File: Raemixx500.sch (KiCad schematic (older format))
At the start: 2 parts

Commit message: Begin adding part numbers
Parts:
- V0, V1: MFG Name (none) -> SKIP; MFG Part Num (none) -> SKIP; Optional (none) -> SKIP
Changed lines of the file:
@@
 F 2 "Symbol:OSHW-Logo2_14.6x12mm_SilkScreen" H 6380 7640 50  0001 C CNN
 F 3 "" H 6380 7640 50  0001 C CNN
+F 4 "SKIP" H 6380 7640 50  0001 C CNN "MFG Name"
+F 5 "SKIP" H 6380 7640 50  0001 C CNN "MFG Part Num"
+F 6 "SKIP" H 6380 7640 50  0001 C CNN "Optional"
 	1    6380 7640
 	1    0    0    -1
@@
 F 2 "Symbol:KiCad-Logo2_12mm_SilkScreen" H 6380 7430 50  0001 C CNN
 F 3 "" H 6380 7430 50  0001 C CNN
+F 4 "SKIP" H 6380 7430 50  0001 C CNN "MFG Name"
+F 5 "SKIP" H 6380 7430 50  0001 C CNN "MFG Part Num"
+F 6 "SKIP" H 6380 7430 50  0001 C CNN "Optional"
 	1    6380 7430
 	1    0    0    -1

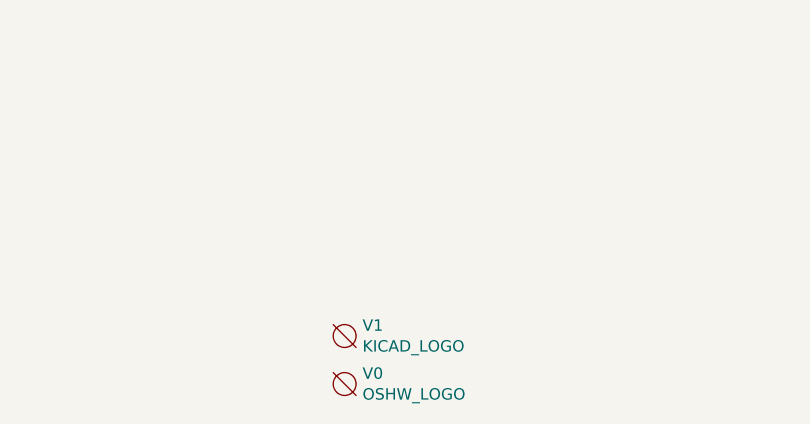
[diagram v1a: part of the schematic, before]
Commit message: Add EMI filter 3D models, add logo, re-add Rock Lobster (closes #15) Thanks to Szabó Zoltán and Workshopshed!
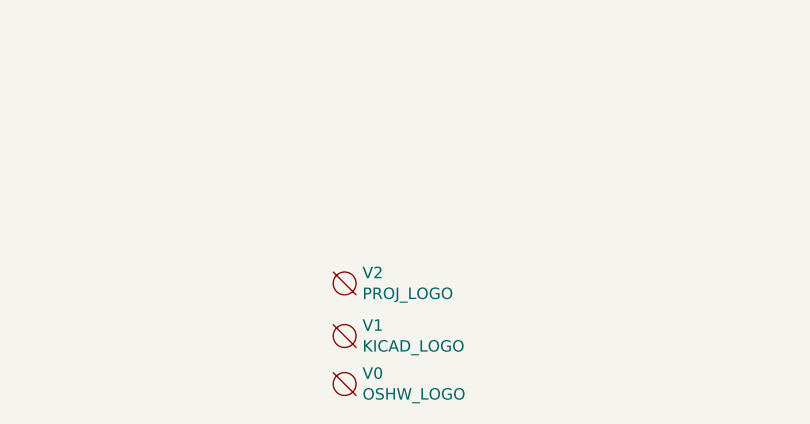
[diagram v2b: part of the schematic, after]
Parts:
- added V2: PROJ_LOGO, Raemixx500:Logo, symbol void:Void
- V1: footprint Symbol:KiCad-Logo2_12mm_SilkScreen -> Symbol:KiCad-Logo2_8mm_SilkScreen
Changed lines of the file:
@@
 F 0 "V1" H 6458 7476 50  0000 L CNN
 F 1 "KICAD_LOGO" H 6458 7385 50  0000 L CNN
-F 2 "Symbol:KiCad-Logo2_12mm_SilkScreen" H 6380 7430 50  0001 C CNN
+F 2 "Symbol:KiCad-Logo2_8mm_SilkScreen" H 6380 7430 50  0001 C CNN
 F 3 "" H 6380 7430 50  0001 C CNN
 F 4 "SKIP" H 6380 7430 50  0001 C CNN "MFG Name"
@@
 	1    0    0    -1
 $EndComp
+$Comp
+L void:Void V2
+U 1 1 5EB0B2BE
+P 6380 7200
+F 0 "V2" H 6458 7246 50  0000 L CNN
+F 1 "PROJ_LOGO" H 6458 7155 50  0000 L CNN
+F 2 "Raemixx500:Logo" H 6380 7200 50  0001 C CNN
+F 3 "" H 6380 7200 50  0001 C CNN
+F 4 "SKIP" H 6380 7200 50  0001 C CNN "MFG Name"
+F 5 "SKIP" H 6380 7200 50  0001 C CNN "MFG Part Num"
+F 6 "SKIP" H 6380 7200 50  0001 C CNN "Optional"
+	1    6380 7200
+	1    0    0    -1
+$EndComp

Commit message: Rename "Optional" Field to "Section"
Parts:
- V0, V1, V2: Optional SKIP -> (none); Section (none) -> SKIP
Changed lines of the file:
@@
 F 4 "SKIP" H 6380 7640 50  0001 C CNN "MFG Name"
 F 5 "SKIP" H 6380 7640 50  0001 C CNN "MFG Part Num"
-F 6 "SKIP" H 6380 7640 50  0001 C CNN "Optional"
+F 6 "SKIP" H 6380 7640 50  0001 C CNN "Section"
 	1    6380 7640
 	1    0    0    -1
@@
 F 4 "SKIP" H 6380 7430 50  0001 C CNN "MFG Name"
 F 5 "SKIP" H 6380 7430 50  0001 C CNN "MFG Part Num"
-F 6 "SKIP" H 6380 7430 50  0001 C CNN "Optional"
+F 6 "SKIP" H 6380 7430 50  0001 C CNN "Section"
 	1    6380 7430
 	1    0    0    -1
@@
 F 4 "SKIP" H 6380 7200 50  0001 C CNN "MFG Name"
 F 5 "SKIP" H 6380 7200 50  0001 C CNN "MFG Part Num"
-F 6 "SKIP" H 6380 7200 50  0001 C CNN "Optional"
+F 6 "SKIP" H 6380 7200 50  0001 C CNN "Section"
 	1    6380 7200
 	1    0    0    -1
